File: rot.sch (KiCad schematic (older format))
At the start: 34 parts, among them J3 543630489, J4 M20-7830642, U2 W25Q32JVSSIQ_TR, U3 W25Q32JVSSIQ_TR, U4 W25Q32JVSSIQ_TR, U5 W25Q32JVSSIQ_TR

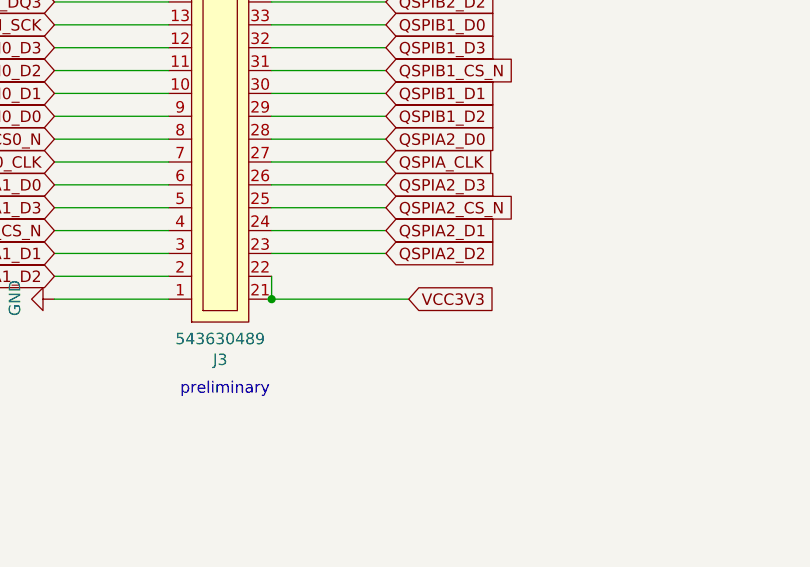
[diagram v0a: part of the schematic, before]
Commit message: Added SPI connector
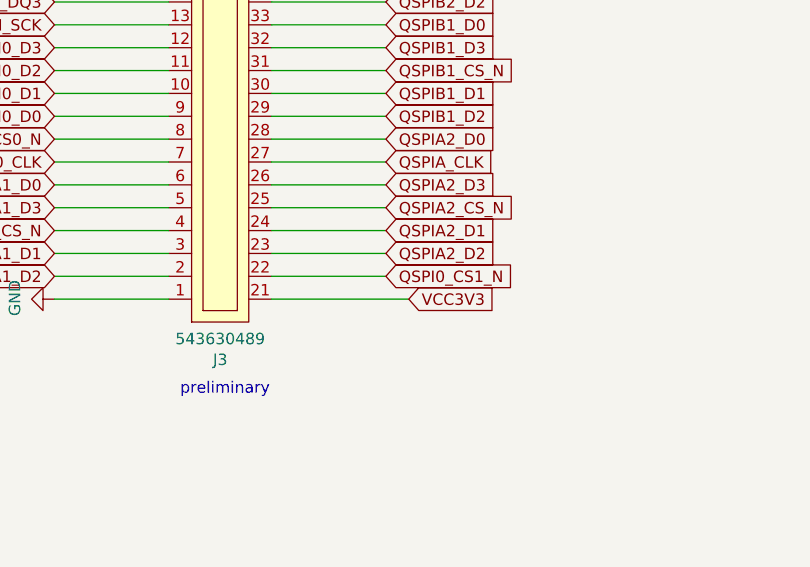
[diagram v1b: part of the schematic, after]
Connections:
- net VCC3V3: no longer J3.22
- new net QSPI0_CS1_N: J3.22
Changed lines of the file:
@@
-$Comp
-L artix-dc-scm:GND #PWR?
-U 1 1 5FD82134
-P 11400 2650
-AR Path="/5FC6B687/5FD82134" Ref="#PWR?"  Part="1"
-AR Path="/624C566F/5FD82134" Ref="#PWR024"  Part="1"
-F 0 "#PWR024" H 11400 2400 50  0001 C CNN
-F 1 "GND" H 11405 2477 50  0000 C CNN
-F 2 "" H 11400 2650 50  0001 C CNN
-F 3 "" H 11400 2650 50  0001 C CNN
-	1    11400 2650
-	1    0    0    -1
-$EndComp
 $Comp
 L artix-dc-scm:GND #PWR?
@@
 Wire Wire Line
 	9175 6525 9775 6525
-Wire Wire Line
-	9175 6425 9175 6525
-Connection ~ 9175 6525
 $Comp
 L artix-dc-scm:543630489 J3
@@
 Wire Wire Line
 	8725 5325 8225 5325
+Wire Wire Line
+	9175 6425 9675 6425
+Text GLabel 9675 6425 2    50   Input ~ 0
+QSPI0_CS1_N
+$Comp
+L artix-dc-scm:GND #PWR?
+U 1 1 5FD82134
+P 11400 2650
+AR Path="/5FC6B687/5FD82134" Ref="#PWR?"  Part="1"
+AR Path="/624C566F/5FD82134" Ref="#PWR024"  Part="1"
+F 0 "#PWR024" H 11400 2400 50  0001 C CNN
+F 1 "GND" H 11405 2477 50  0000 C CNN
+F 2 "" H 11400 2650 50  0001 C CNN
+F 3 "" H 11400 2650 50  0001 C CNN
+	1    11400 2650
+	1    0    0    -1
+$EndComp
 $EndSCHEMATC

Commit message: Added local libs
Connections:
- net FCS_B renamed ROT_QSPI_CS_B
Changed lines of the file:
@@
 	1    0    0    1
 $EndComp
-Text GLabel 9675 4625 2    50   Input ~ 0
-FCS_B
 Text GLabel 8225 5325 0    50   Input ~ 0
 ROT_QSPI_SCK
@@
 	1    0    0    -1
 $EndComp
+Text GLabel 9675 4625 2    50   Input ~ 0
+ROT_QSPI_CS_B
 $EndSCHEMATC
